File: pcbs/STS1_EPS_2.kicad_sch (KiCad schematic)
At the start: 8 parts, among them J1 Inter-EPS, J2 DS1, J3 DS2, J4 DS3, J5 DS4, J6 RBF, J7 Antenna Deployment, J8 UCI

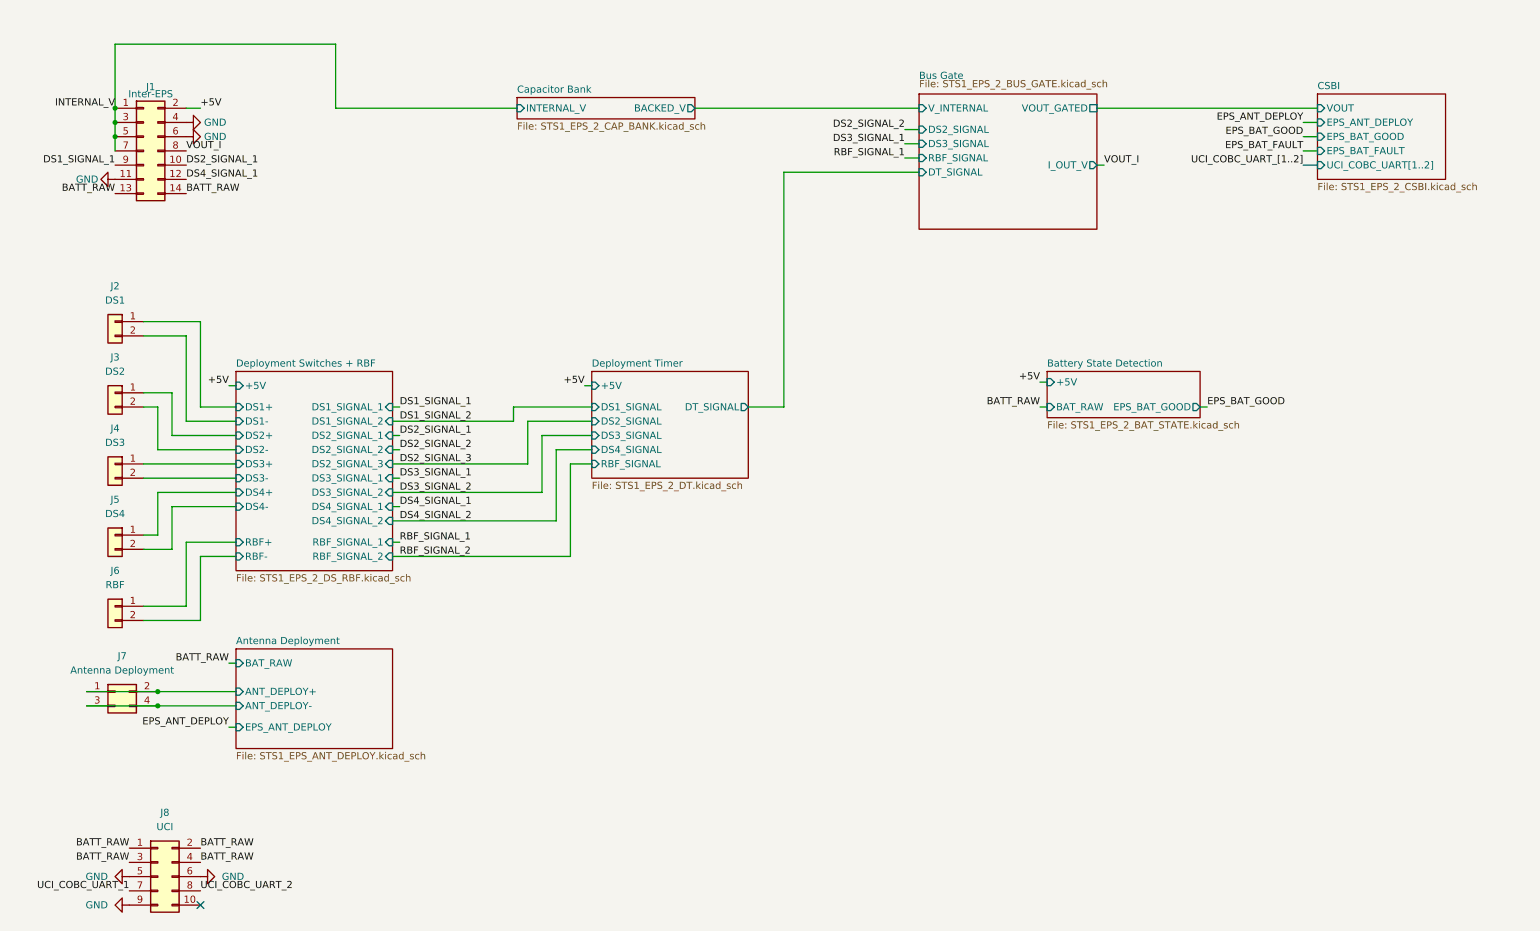
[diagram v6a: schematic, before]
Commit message: Added test points to STS1_EPS_2.
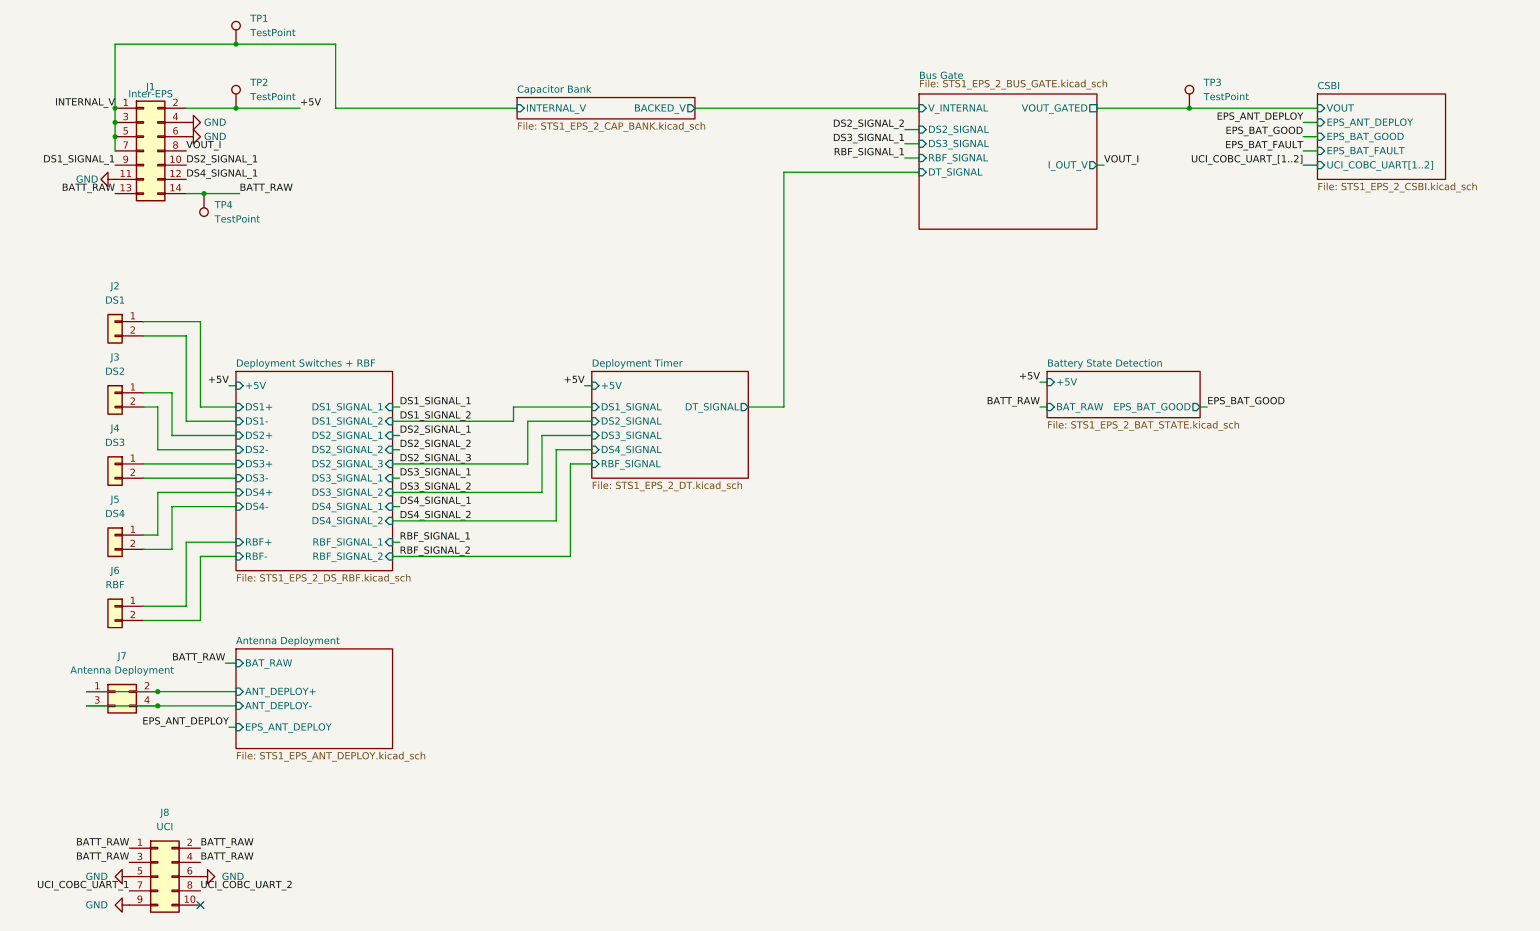
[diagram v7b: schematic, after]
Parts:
- added TP1, TP2, TP3, TP4: TestPoint, TestPoint:TestPoint_THTPad_D1.0mm_Drill0.5mm, symbol Connector:TestPoint
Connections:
- net +5V: now also TP2.1
- net BATT_RAW: now also TP4.1
- net Bus Gate/VOUT_GATED: now also TP3.1
- net INTERNAL_V: now also TP1.1

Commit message: worked on sts1_eps_1
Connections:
- net BATT_RAW: no longer J8.2 (Pin_2), J8.3 (Pin_3), J8.4 (Pin_4)
- net GND: no longer J8.5 (Pin_5), J8.9 (Pin_9)
- net UCI_COBC_UART_1: no longer names the net of J8.7 (Pin_7)
- net UCI_COBC_UART_2: no longer names the net of J8.8 (Pin_8)
- new net GNDREF: J8.2 (Pin_2)
- new net UCI_COBC_3V3: J8.5 (Pin_5)
- new net UCI_COBC_UART_RX: J8.4 (Pin_4)
- new net UCI_COBC_UART_TX: J8.3 (Pin_3)
- no-connect marks 1 -> 4
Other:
- added sheet Battery (STS1_EPS_2_BATTERY.kicad_sch)
